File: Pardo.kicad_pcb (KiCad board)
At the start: 2 copper layers, 50.8 x 22.9 mm, 42 parts, among them J1 USB_OTG, J2 Conn_02x01, J3 Conn_02x01, J4 Conn_02x01, J5 Conn_02x01, J7 Conn_02x01, SW1 SW_Push, U1 ATSAMD21G18A-AUT, U2 TPS73733DCQR, U3 MCP73832T-2ACI_OT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

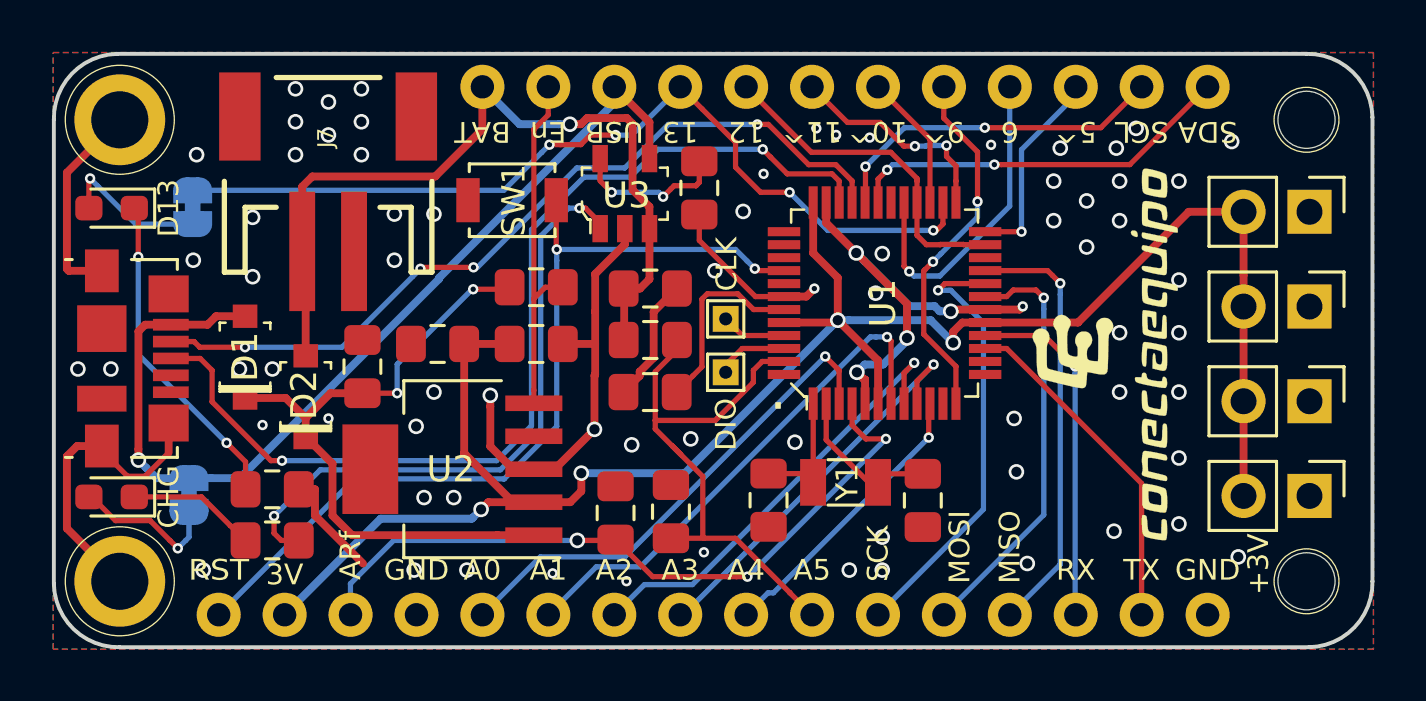
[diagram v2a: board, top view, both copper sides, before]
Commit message: D2 batt schk deleted
Signed-off-by: Ricardo Mena C <rgacort12@gmail.com>
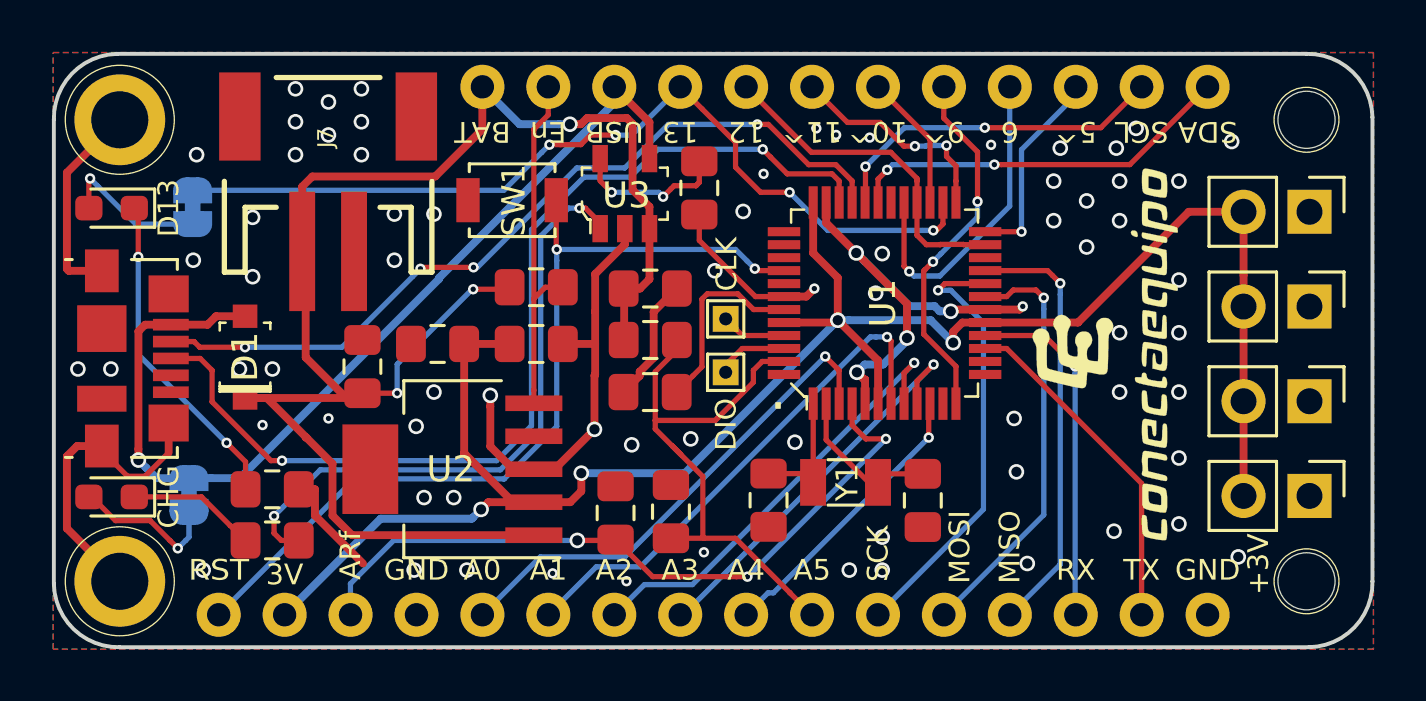
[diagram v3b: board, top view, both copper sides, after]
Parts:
- removed D2: MBR0520LT1G, digikey-footprints:SOD-123
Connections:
- C4-CR1 pad 1: Net-(C4-CR1-Pad1) -> +BATT
- D1 pad K: Net-(C4-CR1-Pad1) -> +BATT
- R1 pad 1: Net-(C4-CR1-Pad1) -> +BATT
- U2 pad 1: Net-(C4-CR1-Pad1) -> +BATT
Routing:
- net +BATT: track 32.0 -> 61.9 mm, vias 1 -> 3
- net Net-(C4-CR1-Pad1): track 25.5 -> 0.00 mm, vias 2 -> 0
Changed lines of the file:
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@@
     (tracks 576)
     (zones 0)
-    (modules 42)
-    (nets 54)
+    (modules 41)
+    (nets 53)
   )
   (page A)
@@
   (net 51 A0)
   (net 52 En)
-  (net 53 "Net-(C4-CR1-Pad1)")
   (net_class Default "This is the default net class."
     (clearance 0.15)
@@
     (add_net "Net-(C2-Pad1)")
     (add_net "Net-(C3-Pad1)")
-    (add_net "Net-(C4-CR1-Pad1)")
     (add_net "Net-(D3.1-Pad1)")
     (add_net "Net-(D3.1-Pad2)")
@@
       (net 52 En))
     (pad 1 smd rect (at -3.1375 -2.54 180) (size 2.2 0.6) (layers F.Cu F.Paste F.Mask)
-      (net 53 "Net-(C4-CR1-Pad1)"))
+      (net 6 +BATT))
     (model ${KISYS3DMOD}/Package_TO_SOT_SMD.3dshapes/SOT-223-6.wrl
       (at (xyz 0 0 0))
@@
     )
     (pad 1 smd roundrect (at -1.025 0 90) (size 1.15 1.4) (layers F.Cu F.Paste F.Mask) (roundrect_rratio 0.217391)
-      (net 53 "Net-(C4-CR1-Pad1)"))
+      (net 6 +BATT))
     (pad 2 smd roundrect (at 1.025 0 90) (size 1.15 1.4) (layers F.Cu F.Paste F.Mask) (roundrect_rratio 0.217391)
       (net 2 GND))
@@
       (net 23 VBUS))
     (pad K smd rect (at -1.575 0 90) (size 0.9 0.95) (layers F.Cu F.Paste F.Mask)
-      (net 53 "Net-(C4-CR1-Pad1)"))
-    (model ${KISYS3DMOD}/Diode_SMD.3dshapes/D_SOD-123F.step
-      (at (xyz 0 0 0))
-      (scale (xyz 1 1 1))
-      (rotate (xyz 0 0 0))
-    )
-  )
-  (module digikey-footprints:SOD-123 (layer F.Cu)
-    (at 133.9215 94.9577 90)
-    (attr smd)
-    (fp_text reference D2 (at 0.0635 -0.0635 270) (layer F.SilkS)
-      (effects (font (size 1 1) (thickness 0.15)))
-    )
-    (fp_text value MBR0520LT1G (at -25.806001 3.185499 180) (layer F.Fab)
-      (effects (font (size 1 1) (thickness 0.15)))
-    )
-    (fp_line (start -0.975 0.975) (end -1.325 0.975) (layer F.SilkS) (width 0.1))
-    (fp_text user %R (at 0 0 90) (layer F.Fab)
-      (effects (font (size 0.5 0.5) (thickness 0.075)))
-    )
-    (fp_line (start 3.175 -1.15) (end -3.175 -1.15) (layer F.CrtYd) (width 0.05))
-    (fp_line (start -3.175 1.15) (end -3.175 -1.15) (layer F.CrtYd) (width 0.05))
-    (fp_line (start 3.175 1.15) (end -3.175 1.15) (layer F.CrtYd) (width 0.05))
-    (fp_line (start 3.175 -1.15) (end 3.175 1.15) (layer F.CrtYd) (width 0.05))
-    (fp_line (start -0.975 -0.975) (end -1.325 -0.975) (layer F.SilkS) (width 0.1))
-    (fp_line (start -1.325 -0.975) (end -1.325 0.975) (layer F.SilkS) (width 0.1))
-    (fp_line (start 1.325 0.725) (end 1.325 0.975) (layer F.SilkS) (width 0.1))
-    (fp_line (start 1.325 0.975) (end 1.075 0.975) (layer F.SilkS) (width 0.1))
-    (fp_line (start 1.025 -0.975) (end 1.325 -0.975) (layer F.SilkS) (width 0.1))
-    (fp_line (start 1.325 -0.975) (end 1.325 -0.75) (layer F.SilkS) (width 0.1))
-    (fp_line (start -1.325 0.85) (end 1.325 0.85) (layer F.Fab) (width 0.1))
-    (fp_line (start -1.325 -0.85) (end -1.325 0.85) (layer F.Fab) (width 0.1))
-    (fp_line (start 1.325 -0.85) (end 1.325 0.85) (layer F.Fab) (width 0.1))
-    (fp_line (start -1.325 -0.85) (end 1.325 -0.85) (layer F.Fab) (width 0.1))
-    (fp_line (start -1.225 -0.975) (end -1.225 0.975) (layer F.SilkS) (width 0.1))
-    (fp_line (start -1.125 -0.975) (end -1.125 0.975) (layer F.SilkS) (width 0.1))
-    (pad K smd rect (at -1.575 0 90) (size 0.9 0.95) (layers F.Cu F.Paste F.Mask)
-      (net 53 "Net-(C4-CR1-Pad1)"))
-    (pad A smd rect (at 1.575 0 90) (size 0.9 0.95) (layers F.Cu F.Paste F.Mask)
       (net 6 +BATT))
     (model ${KISYS3DMOD}/Diode_SMD.3dshapes/D_SOD-123F.step
@@
       (net 52 En))
     (pad 1 smd roundrect (at -1.025 0) (size 1.15 1.4) (layers F.Cu F.Paste F.Mask) (roundrect_rratio 0.217391)
-      (net 53 "Net-(C4-CR1-Pad1)"))
+      (net 6 +BATT))
     (model ${KISYS3DMOD}/Resistor_SMD.3dshapes/R_0805_2012Metric.wrl
       (at (xyz 0 0 0))
@@
   (segment (start 167.943601 87.834399) (end 170.053 87.834399) (width 0.3032) (layer F.Cu) (net 5))
   (segment (start 163.6769 92.1011) (end 167.943601 87.834399) (width 0.3032) (layer F.Cu) (net 5))
-  (segment (start 133.9215 89.49436) (end 133.78688 89.35974) (width 0.3032) (layer F.Cu) (net 6))
-  (segment (start 133.9215 93.3827) (end 133.9215 89.49436) (width 0.3032) (layer F.Cu) (net 6))
   (segment (start 133.78688 86.86292) (end 133.78688 89.35974) (width 0.3032) (layer F.Cu) (net 6))
   (segment (start 140.7247 84.662792) (end 138.913192 86.4743) (width 0.3032) (layer F.Cu) (net 6))
@@
   (segment (start 142.7107 84.65553) (end 142.7107 91.1833) (width 0.2032) (layer F.Cu) (net 52))
   (segment (start 143.2647 84.10153) (end 143.2647 83.0239) (width 0.2032) (layer F.Cu) (net 52))
-  (segment (start 133.9215 95.7795) (end 133.9215 96.5327) (width 0.3032) (layer F.Cu) (net 53))
-  (segment (start 133.1507 95.0087) (end 133.9215 95.7795) (width 0.3032) (layer F.Cu) (net 53))
-  (segment (start 131.5847 95.0087) (end 133.1507 95.0087) (width 0.3032) (layer F.Cu) (net 53))
-  (segment (start 134.8775 94.8235) (end 133.9215 95.7795) (width 0.3032) (layer F.Cu) (net 53))
-  (segment (start 133.9465 96.5327) (end 134.95351 97.53971) (width 0.3032) (layer F.Cu) (net 53))
-  (segment (start 135.7042 100.2919) (end 141.3075 100.2919) (width 0.3032) (layer F.Cu) (net 53))
-  (segment (start 134.95351 99.54121) (end 135.7042 100.2919) (width 0.3032) (layer F.Cu) (net 53))
-  (segment (start 134.95351 97.53971) (end 134.95351 99.54121) (width 0.3032) (layer F.Cu) (net 53))
-  (segment (start 141.3075 100.2919) (end 142.7107 100.2919) (width 0.3032) (layer F.Cu) (net 53))
-  (segment (start 133.9215 96.5327) (end 133.9465 96.5327) (width 0.3032) (layer F.Cu) (net 53))
-  (segment (start 136.1059 94.8235) (end 134.8775 94.8235) (width 0.3032) (layer F.Cu) (net 53))
-  (segment (start 136.1059 94.8235) (end 137.4447 94.8235) (width 0.2032) (layer F.Cu) (net 53))
-  (segment (start 137.4447 94.8235) (end 137.4447 93.708) (width 0.2032) (layer B.Cu) (net 53))
-  (via (at 140.3731 90.8177) (size 0.4) (drill 0.2032) (layers F.Cu B.Cu) (net 53))
-  (segment (start 140.335 90.8177) (end 140.3731 90.8177) (width 0.2032) (layer B.Cu) (net 53))
-  (segment (start 137.4447 93.708) (end 140.335 90.8177) (width 0.2032) (layer B.Cu) (net 53))
-  (segment (start 141.7013 90.8177) (end 141.7775 90.7415) (width 0.2032) (layer F.Cu) (net 53))
-  (segment (start 140.3731 90.8177) (end 141.7013 90.8177) (width 0.2032) (layer F.Cu) (net 53))
-  (via (at 137.4447 94.8235) (size 0.4) (drill 0.2032) (layers F.Cu B.Cu) (net 53))
+  (segment (start 136.1059 94.8235) (end 137.4447 94.8235) (width 0.2032) (layer F.Cu) (net 6))
+  (segment (start 137.4447 94.8235) (end 137.4447 93.708) (width 0.2032) (layer B.Cu) (net 6))
+  (via (at 140.3731 90.8177) (size 0.4) (drill 0.2032) (layers F.Cu B.Cu) (net 6))
+  (segment (start 140.335 90.8177) (end 140.3731 90.8177) (width 0.2032) (layer B.Cu) (net 6))
+  (segment (start 137.4447 93.708) (end 140.335 90.8177) (width 0.2032) (layer B.Cu) (net 6))
+  (segment (start 141.7013 90.8177) (end 141.7775 90.7415) (width 0.2032) (layer F.Cu) (net 6))
+  (segment (start 140.3731 90.8177) (end 141.7013 90.8177) (width 0.2032) (layer F.Cu) (net 6))
+  (via (at 137.4447 94.8235) (size 0.4) (drill 0.2032) (layers F.Cu B.Cu) (net 6))
+  (segment (start 133.9465 96.5327) (end 133.9215 96.5327) (width 0.3032) (layer F.Cu) (net 6))
+  (segment (start 142.7107 100.2919) (end 135.7042 100.2919) (width 0.3032) (layer F.Cu) (net 6))
+  (segment (start 134.95351 97.53971) (end 133.9465 96.5327) (width 0.3032) (layer F.Cu) (net 6))
+  (segment (start 135.7042 100.2919) (end 134.95351 99.54121) (width 0.3032) (layer F.Cu) (net 6))
+  (segment (start 134.95351 99.54121) (end 134.95351 97.53971) (width 0.3032) (layer F.Cu) (net 6))
+  (segment (start 135.9207 95.0087) (end 136.1059 94.8235) (width 0.3032) (layer F.Cu) (net 6))
+  (segment (start 131.5847 95.0087) (end 135.9207 95.0087) (width 0.3032) (layer F.Cu) (net 6))
+  (segment (start 132.4225 95.0087) (end 131.5847 95.0087) (width 0.3032) (layer F.Cu) (net 6))
+  (segment (start 133.9465 96.5327) (end 132.4225 95.0087) (width 0.3032) (layer F.Cu) (net 6))
+  (segment (start 133.9215 93.4466) (end 135.4836 95.0087) (width 0.3032) (layer F.Cu) (net 6))
+  (segment (start 133.9215 89.49436) (end 133.9215 93.4466) (width 0.3032) (layer F.Cu) (net 6))
+  (segment (start 135.4836 95.0087) (end 135.9207 95.0087) (width 0.3032) (layer F.Cu) (net 6))
+  (segment (start 133.78688 89.35974) (end 133.9215 89.49436) (width 0.3032) (layer F.Cu) (net 6))
   (zone (net 2) (net_name GND) (layer F.Cu) (hatch edge 0.508)
     (connect_pads (clearance 0.254))

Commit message: Pardo fab 1
Signed-off-by: Ricardo Mena C <rgacort12@gmail.com>
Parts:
- added D2: MBR0520LT1G, digikey-footprints:SOD-123, F.Cu at (133.9, 94.6)
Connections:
- C4-CR1 pad 1: +BATT -> Net-(C4-CR1-Pad1)
- D1 pad K: +BATT -> Net-(C4-CR1-Pad1)
- R1 pad 1: +BATT -> Net-(C4-CR1-Pad1)
- U2 pad 1: +BATT -> Net-(C4-CR1-Pad1)
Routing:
- net +BATT: track 61.9 -> 32.0 mm, vias 3 -> 1
- net Net-(C4-CR1-Pad1): track 0.00 -> 25.5 mm, vias 0 -> 2
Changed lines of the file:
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@@
-(kicad_pcb (version 20171130) (host pcbnew 5.0.2+dfsg1-1~bpo9+1)
+(kicad_pcb (version 20171130) (host pcbnew 5.0.2+dfsg1-1)
   (general
     (thickness 1.6)
@@
     (tracks 576)
     (zones 0)
-    (modules 41)
-    (nets 53)
+    (modules 42)
+    (nets 54)
   )
   (page A)
@@
   (net 51 A0)
   (net 52 En)
+  (net 53 "Net-(C4-CR1-Pad1)")
   (net_class Default "This is the default net class."
     (clearance 0.15)
@@
     (add_net "Net-(C2-Pad1)")
     (add_net "Net-(C3-Pad1)")
+    (add_net "Net-(C4-CR1-Pad1)")
     (add_net "Net-(D3.1-Pad1)")
     (add_net "Net-(D3.1-Pad2)")
@@
       (net 52 En))
     (pad 1 smd rect (at -3.1375 -2.54 180) (size 2.2 0.6) (layers F.Cu F.Paste F.Mask)
-      (net 6 +BATT))
+      (net 53 "Net-(C4-CR1-Pad1)"))
     (model ${KISYS3DMOD}/Package_TO_SOT_SMD.3dshapes/SOT-223-6.wrl
       (at (xyz 0 0 0))
@@
     )
     (pad 1 smd roundrect (at -1.025 0 90) (size 1.15 1.4) (layers F.Cu F.Paste F.Mask) (roundrect_rratio 0.217391)
-      (net 6 +BATT))
+      (net 53 "Net-(C4-CR1-Pad1)"))
     (pad 2 smd roundrect (at 1.025 0 90) (size 1.15 1.4) (layers F.Cu F.Paste F.Mask) (roundrect_rratio 0.217391)
       (net 2 GND))
@@
       (net 23 VBUS))
     (pad K smd rect (at -1.575 0 90) (size 0.9 0.95) (layers F.Cu F.Paste F.Mask)
-      (net 6 +BATT))
+      (net 53 "Net-(C4-CR1-Pad1)"))
     (model ${KISYS3DMOD}/Diode_SMD.3dshapes/D_SOD-123F.step
       (at (xyz 0 0 0))
@@
       (net 52 En))
     (pad 1 smd roundrect (at -1.025 0) (size 1.15 1.4) (layers F.Cu F.Paste F.Mask) (roundrect_rratio 0.217391)
-      (net 6 +BATT))
+      (net 53 "Net-(C4-CR1-Pad1)"))
     (model ${KISYS3DMOD}/Resistor_SMD.3dshapes/R_0805_2012Metric.wrl
       (at (xyz 0 0 0))
@@
     (pad 1 np_thru_hole circle (at 0 0 90) (size 2.2 2.2) (drill 2.2) (layers *.Cu *.Mask))
   )
+  (module digikey-footprints:SOD-123 (layer F.Cu)
+    (at 133.8834 94.6277 90)
+    (attr smd)
+    (fp_text reference D2 (at 0 0.0508 90) (layer F.SilkS)
+      (effects (font (size 1 1) (thickness 0.15)))
+    )
+    (fp_text value MBR0520LT1G (at 0.07 2.05 90) (layer F.Fab)
+      (effects (font (size 1 1) (thickness 0.15)))
+    )
+    (fp_line (start -0.975 0.975) (end -1.325 0.975) (layer F.SilkS) (width 0.1))
+    (fp_text user %R (at 0 0 90) (layer F.Fab)
+      (effects (font (size 0.5 0.5) (thickness 0.075)))
+    )
+    (fp_line (start 3.175 -1.15) (end -3.175 -1.15) (layer F.CrtYd) (width 0.05))
+    (fp_line (start -3.175 1.15) (end -3.175 -1.15) (layer F.CrtYd) (width 0.05))
+    (fp_line (start 3.175 1.15) (end -3.175 1.15) (layer F.CrtYd) (width 0.05))
+    (fp_line (start 3.175 -1.15) (end 3.175 1.15) (layer F.CrtYd) (width 0.05))
+    (fp_line (start -0.975 -0.975) (end -1.325 -0.975) (layer F.SilkS) (width 0.1))
+    (fp_line (start -1.325 -0.975) (end -1.325 0.975) (layer F.SilkS) (width 0.1))
+    (fp_line (start 1.325 0.725) (end 1.325 0.975) (layer F.SilkS) (width 0.1))
+    (fp_line (start 1.325 0.975) (end 1.075 0.975) (layer F.SilkS) (width 0.1))
+    (fp_line (start 1.025 -0.975) (end 1.325 -0.975) (layer F.SilkS) (width 0.1))
+    (fp_line (start 1.325 -0.975) (end 1.325 -0.75) (layer F.SilkS) (width 0.1))
+    (fp_line (start -1.325 0.85) (end 1.325 0.85) (layer F.Fab) (width 0.1))
+    (fp_line (start -1.325 -0.85) (end -1.325 0.85) (layer F.Fab) (width 0.1))
+    (fp_line (start 1.325 -0.85) (end 1.325 0.85) (layer F.Fab) (width 0.1))
+    (fp_line (start -1.325 -0.85) (end 1.325 -0.85) (layer F.Fab) (width 0.1))
+    (fp_line (start -1.225 -0.975) (end -1.225 0.975) (layer F.SilkS) (width 0.1))
+    (fp_line (start -1.125 -0.975) (end -1.125 0.975) (layer F.SilkS) (width 0.1))
+    (pad K smd rect (at -1.575 0 90) (size 0.9 0.95) (layers F.Cu F.Paste F.Mask)
+      (net 53 "Net-(C4-CR1-Pad1)"))
+    (pad A smd rect (at 1.575 0 90) (size 0.9 0.95) (layers F.Cu F.Paste F.Mask)
+      (net 6 +BATT))
+  )
   (gr_text . (at 152.1206 94.7293) (layer F.SilkS)
     (effects (font (size 1.5 1.5) (thickness 0.3)))
@@
   (segment (start 147.1651 89.3129) (end 147.1651 88.4847) (width 0.3032) (layer F.Cu) (net 6))
   (segment (start 146.1717 90.7923) (end 146.7993 90.7923) (width 0.3032) (layer F.Cu) (net 6))
+  (segment (start 133.9215 89.49436) (end 133.78688 89.35974) (width 0.3032) (layer F.Cu) (net 6))
+  (segment (start 133.9215 93.3827) (end 133.9215 89.49436) (width 0.3032) (layer F.Cu) (net 6))
   (segment (start 148.0439 96.857202) (end 149.2213 98.034602) (width 0.2032) (layer F.Cu) (net 7))
   (segment (start 148.37949 97.192792) (end 148.0439 96.857202) (width 0.2032) (layer F.Cu) (net 7))
@@
   (segment (start 142.7107 84.65553) (end 142.7107 91.1833) (width 0.2032) (layer F.Cu) (net 52))
   (segment (start 143.2647 84.10153) (end 143.2647 83.0239) (width 0.2032) (layer F.Cu) (net 52))
-  (segment (start 136.1059 94.8235) (end 137.4447 94.8235) (width 0.2032) (layer F.Cu) (net 6))
-  (segment (start 137.4447 94.8235) (end 137.4447 93.708) (width 0.2032) (layer B.Cu) (net 6))
-  (via (at 140.3731 90.8177) (size 0.4) (drill 0.2032) (layers F.Cu B.Cu) (net 6))
-  (segment (start 140.335 90.8177) (end 140.3731 90.8177) (width 0.2032) (layer B.Cu) (net 6))
-  (segment (start 137.4447 93.708) (end 140.335 90.8177) (width 0.2032) (layer B.Cu) (net 6))
-  (segment (start 141.7013 90.8177) (end 141.7775 90.7415) (width 0.2032) (layer F.Cu) (net 6))
-  (segment (start 140.3731 90.8177) (end 141.7013 90.8177) (width 0.2032) (layer F.Cu) (net 6))
-  (via (at 137.4447 94.8235) (size 0.4) (drill 0.2032) (layers F.Cu B.Cu) (net 6))
-  (segment (start 133.9465 96.5327) (end 133.9215 96.5327) (width 0.3032) (layer F.Cu) (net 6))
-  (segment (start 142.7107 100.2919) (end 135.7042 100.2919) (width 0.3032) (layer F.Cu) (net 6))
-  (segment (start 134.95351 97.53971) (end 133.9465 96.5327) (width 0.3032) (layer F.Cu) (net 6))
-  (segment (start 135.7042 100.2919) (end 134.95351 99.54121) (width 0.3032) (layer F.Cu) (net 6))
-  (segment (start 134.95351 99.54121) (end 134.95351 97.53971) (width 0.3032) (layer F.Cu) (net 6))
-  (segment (start 135.9207 95.0087) (end 136.1059 94.8235) (width 0.3032) (layer F.Cu) (net 6))
-  (segment (start 131.5847 95.0087) (end 135.9207 95.0087) (width 0.3032) (layer F.Cu) (net 6))
-  (segment (start 132.4225 95.0087) (end 131.5847 95.0087) (width 0.3032) (layer F.Cu) (net 6))
-  (segment (start 133.9465 96.5327) (end 132.4225 95.0087) (width 0.3032) (layer F.Cu) (net 6))
-  (segment (start 133.9215 93.4466) (end 135.4836 95.0087) (width 0.3032) (layer F.Cu) (net 6))
-  (segment (start 133.9215 89.49436) (end 133.9215 93.4466) (width 0.3032) (layer F.Cu) (net 6))
-  (segment (start 135.4836 95.0087) (end 135.9207 95.0087) (width 0.3032) (layer F.Cu) (net 6))
-  (segment (start 133.78688 89.35974) (end 133.9215 89.49436) (width 0.3032) (layer F.Cu) (net 6))
+  (segment (start 136.1059 94.8235) (end 137.4447 94.8235) (width 0.2032) (layer F.Cu) (net 53))
+  (segment (start 137.4447 94.8235) (end 137.4447 93.708) (width 0.2032) (layer B.Cu) (net 53))
+  (via (at 140.3731 90.8177) (size 0.4) (drill 0.2032) (layers F.Cu B.Cu) (net 53))
+  (segment (start 140.335 90.8177) (end 140.3731 90.8177) (width 0.2032) (layer B.Cu) (net 53))
+  (segment (start 137.4447 93.708) (end 140.335 90.8177) (width 0.2032) (layer B.Cu) (net 53))
+  (segment (start 141.7013 90.8177) (end 141.7775 90.7415) (width 0.2032) (layer F.Cu) (net 53))
+  (segment (start 140.3731 90.8177) (end 141.7013 90.8177) (width 0.2032) (layer F.Cu) (net 53))
+  (via (at 137.4447 94.8235) (size 0.4) (drill 0.2032) (layers F.Cu B.Cu) (net 53))
+  (segment (start 134.95351 99.54121) (end 135.7042 100.2919) (width 0.3032) (layer F.Cu) (net 53))
+  (segment (start 134.95351 97.53971) (end 134.95351 99.54121) (width 0.3032) (layer F.Cu) (net 53))
+  (segment (start 135.7042 100.2919) (end 141.3075 100.2919) (width 0.3032) (layer F.Cu) (net 53))
+  (segment (start 141.3075 100.2919) (end 142.7107 100.2919) (width 0.3032) (layer F.Cu) (net 53))
+  (segment (start 133.9465 96.5327) (end 134.95351 97.53971) (width 0.3032) (layer F.Cu) (net 53))
+  (segment (start 133.9215 96.5327) (end 133.9465 96.5327) (width 0.3032) (layer F.Cu) (net 53))
+  (segment (start 133.9215 95.7795) (end 133.9215 96.5327) (width 0.3032) (layer F.Cu) (net 53))
+  (segment (start 136.1059 94.8235) (end 134.8775 94.8235) (width 0.3032) (layer F.Cu) (net 53))
+  (segment (start 131.5847 95.0087) (end 133.1507 95.0087) (width 0.3032) (layer F.Cu) (net 53))
+  (segment (start 133.1507 95.0087) (end 133.9215 95.7795) (width 0.3032) (layer F.Cu) (net 53))
+  (segment (start 134.8775 94.8235) (end 133.9215 95.7795) (width 0.3032) (layer F.Cu) (net 53))
   (zone (net 2) (net_name GND) (layer F.Cu) (hatch edge 0.508)
     (connect_pads (clearance 0.254))
